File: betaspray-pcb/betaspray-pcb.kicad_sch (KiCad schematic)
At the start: 11 parts, among them SW1 SW_Push, SW2 SW_Push, U1 ESP32-S3-WROOM-1

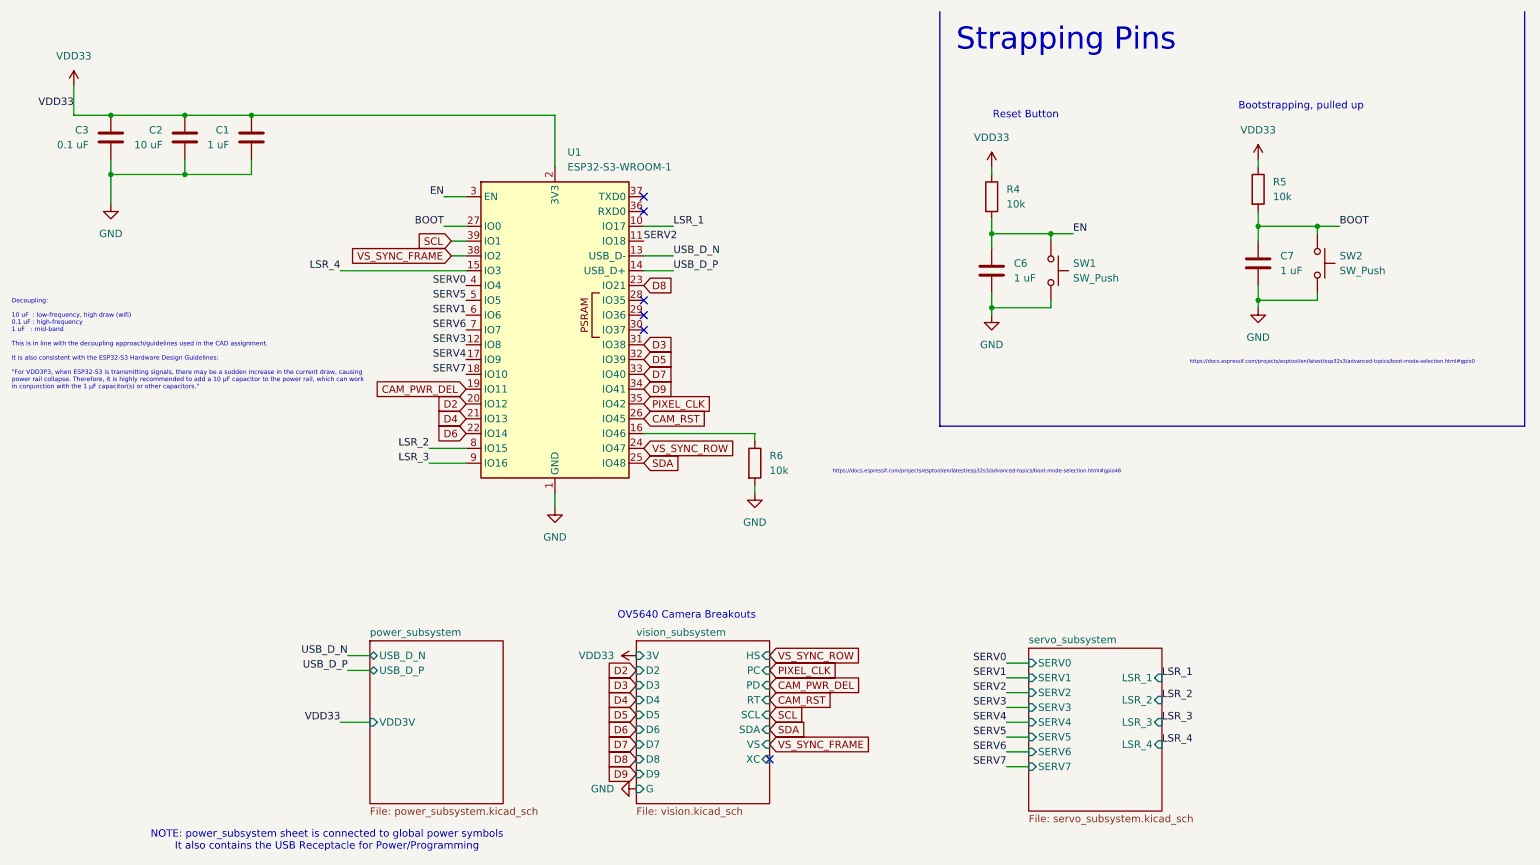
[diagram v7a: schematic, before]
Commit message: Change Laser diode layout
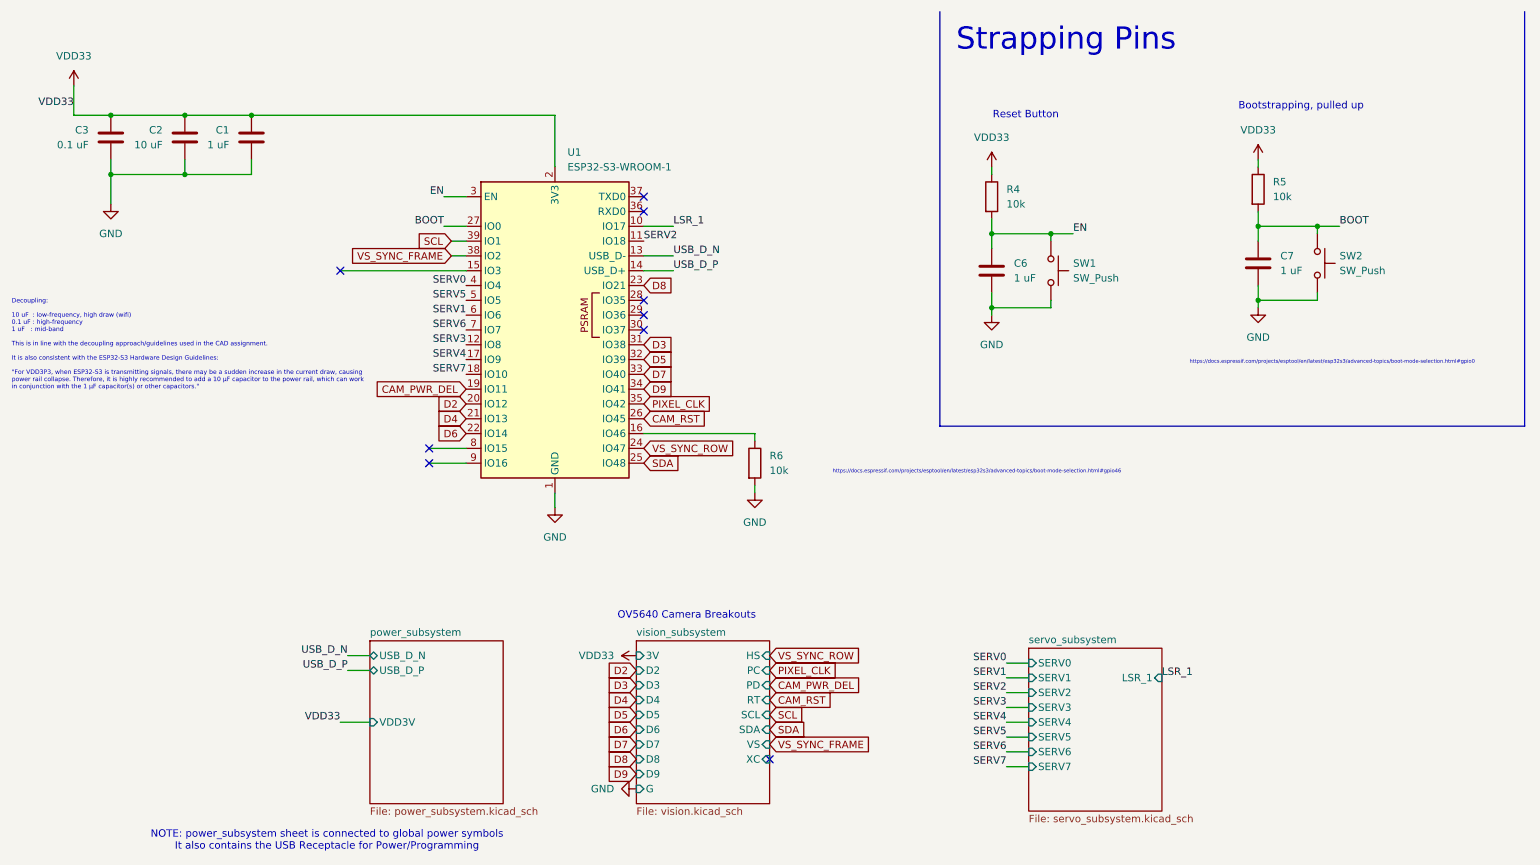
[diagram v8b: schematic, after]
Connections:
- net LSR_2: no longer names the net of U1.8 (IO15)
- net LSR_3: no longer names the net of U1.9 (IO16)
- net LSR_4: no longer names the net of U1.15 (IO3)
- no-connect marks 6 -> 9
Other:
- sheet servo_subsystem ports: added none; removed LSR_2, LSR_3, LSR_4
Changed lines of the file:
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@@
 	)
 	(no_connect
+		(at 74.93 55.88)
+	)
+	(no_connect
 		(at 127 45.72)
 	)
@@
 	)
 	(no_connect
+		(at 90.17 88.9)
+	)
+	(no_connect
+		(at 90.17 86.36)
+	)
+	(no_connect
 		(at 127 63.5)
 	)
@@
 		)
 	)
-	(label "LSR_3"
-		(at 90.17 88.9 180)
-		(effects
-			(font
-				(size 1.27 1.27)
-			)
-			(justify right bottom)
-		)
-	)
 	(label "EN"
 		(at 200.66 49.53 0)
@@
 		)
 	)
-	(label "LSR_4"
-		(at 74.93 55.88 180)
-		(effects
-			(font
-				(size 1.27 1.27)
-			)
-			(justify right bottom)
-		)
-	)
 	(label "SERV1"
 		(at 189.23 125.73 180)
@@
 		)
 	)
-	(label "LSR_2"
-		(at 90.17 86.36 180)
-		(effects
-			(font
-				(size 1.27 1.27)
-			)
-			(justify right bottom)
-		)
-	)
 	(label "SERV6"
 		(at 96.52 66.04 180)
@@
 		)
 	)
-	(label "LSR_2"
-		(at 215.9 129.54 0)
-		(effects
-			(font
-				(size 1.27 1.27)
-			)
-			(justify left bottom)
-		)
-	)
 	(label "SERV3"
 		(at 189.23 130.81 180)
@@
 		)
 	)
-	(label "LSR_4"
-		(at 215.9 137.16 0)
-		(effects
-			(font
-				(size 1.27 1.27)
-			)
-			(justify left bottom)
-		)
-	)
-	(label "LSR_3"
-		(at 215.9 133.35 0)
-		(effects
-			(font
-				(size 1.27 1.27)
-			)
-			(justify left bottom)
-		)
-	)
 	(label "BOOT"
 		(at 246.38 48.26 0)
@@
 			(effects
 				(font
-					(size 1.27 1.27)
-				)
-				(justify right)
-			)
-		)
-		(pin "LSR_2" input
-			(at 215.9 129.54 0)
-			(effects
-				(font
-					(size 1.27 1.27)
-				)
-				(justify right)
-			)
-		)
-		(pin "LSR_3" input
-			(at 215.9 133.35 0)
-			(effects
-				(font
-					(size 1.27 1.27)
-				)
-				(justify right)
-			)
-		)
-		(pin "LSR_4" input
-			(at 215.9 137.16 0)
-			(effects
-				(font
